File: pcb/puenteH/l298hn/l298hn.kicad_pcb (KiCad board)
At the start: 2 copper layers, 48.6 x 86.2 mm, 19 parts, among them K1 CONN_3, K2 CONN_3, P1 CONN_2X2, P2 PWR, P3 CONN_2, P4 CONN_2, U1 L298

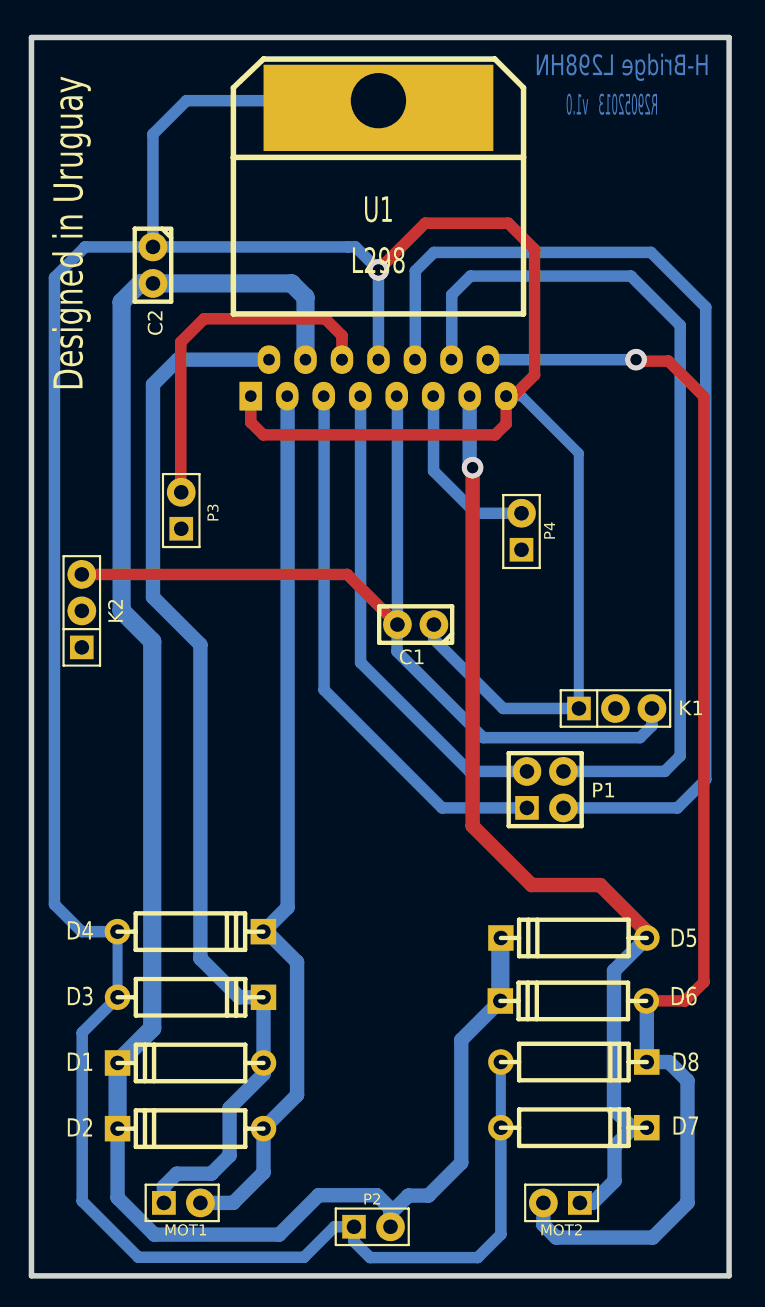
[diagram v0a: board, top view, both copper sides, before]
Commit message: Add pull down in shield motors (pins HK15 and HK16) for compatibility with usb4butia v1.8.8
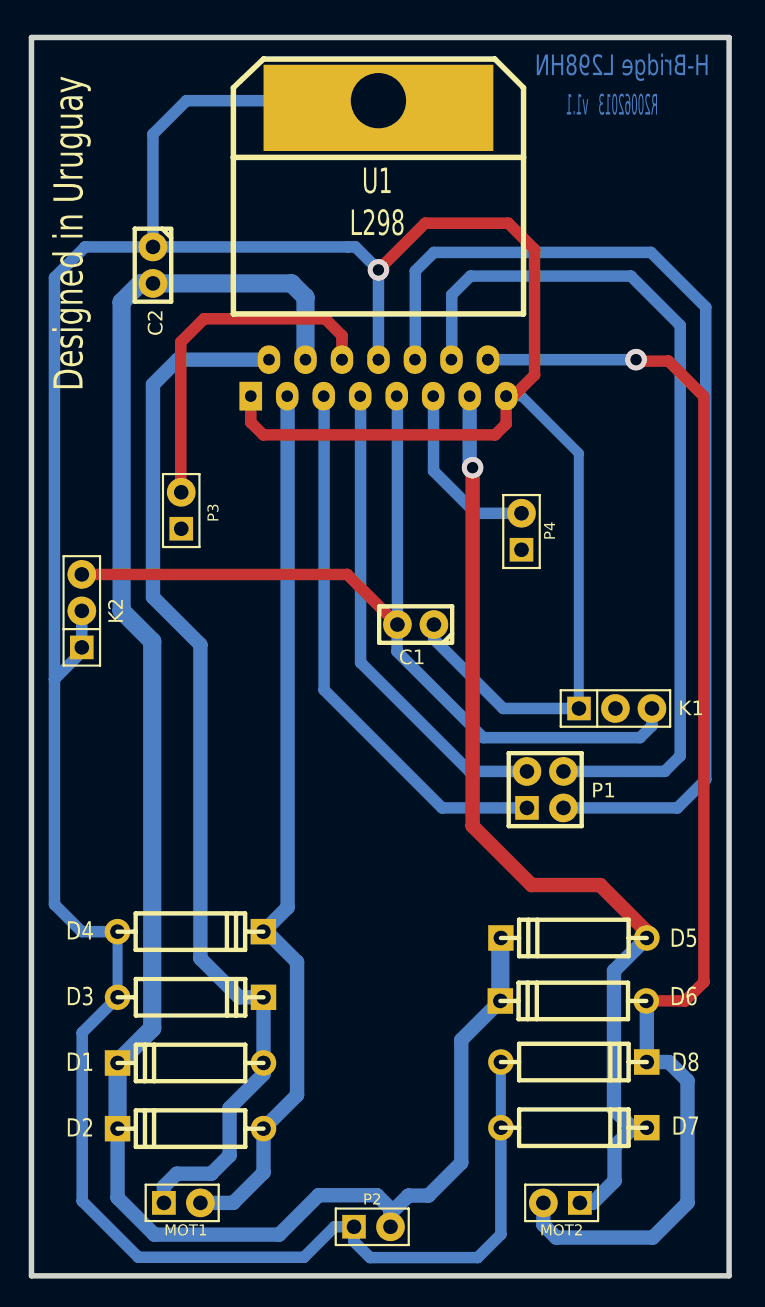
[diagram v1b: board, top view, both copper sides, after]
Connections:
- K1 pad 2: (no net) -> N-0000014
- K2 pad 1: (no net) -> GND
- K2 pad 2: (no net) -> GND
- P3 pad 1: (no net) -> N-000007
- P4 pad 1: (no net) -> N-0000016
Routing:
- net GND: track 252.9 -> 258.4 mm, vias 3 -> 5
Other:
- board text added: "R20062013 v1.1"
- board text removed: "R29052013 v1.0"
